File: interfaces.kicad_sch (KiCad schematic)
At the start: 84 parts, among them IC1 TPD8S009DSMR, J1 WE_629105150521, J2 685119134923, J3 1140084168, Q1 BSS138APW, Q2 BSS138APW, Q3 BSS138APW, Q4 BSS138APW, Q5 BSS138APW, U4 FT4232H-56Q, Y1 ABM8G-12.000MHZ-18-D2Y-T

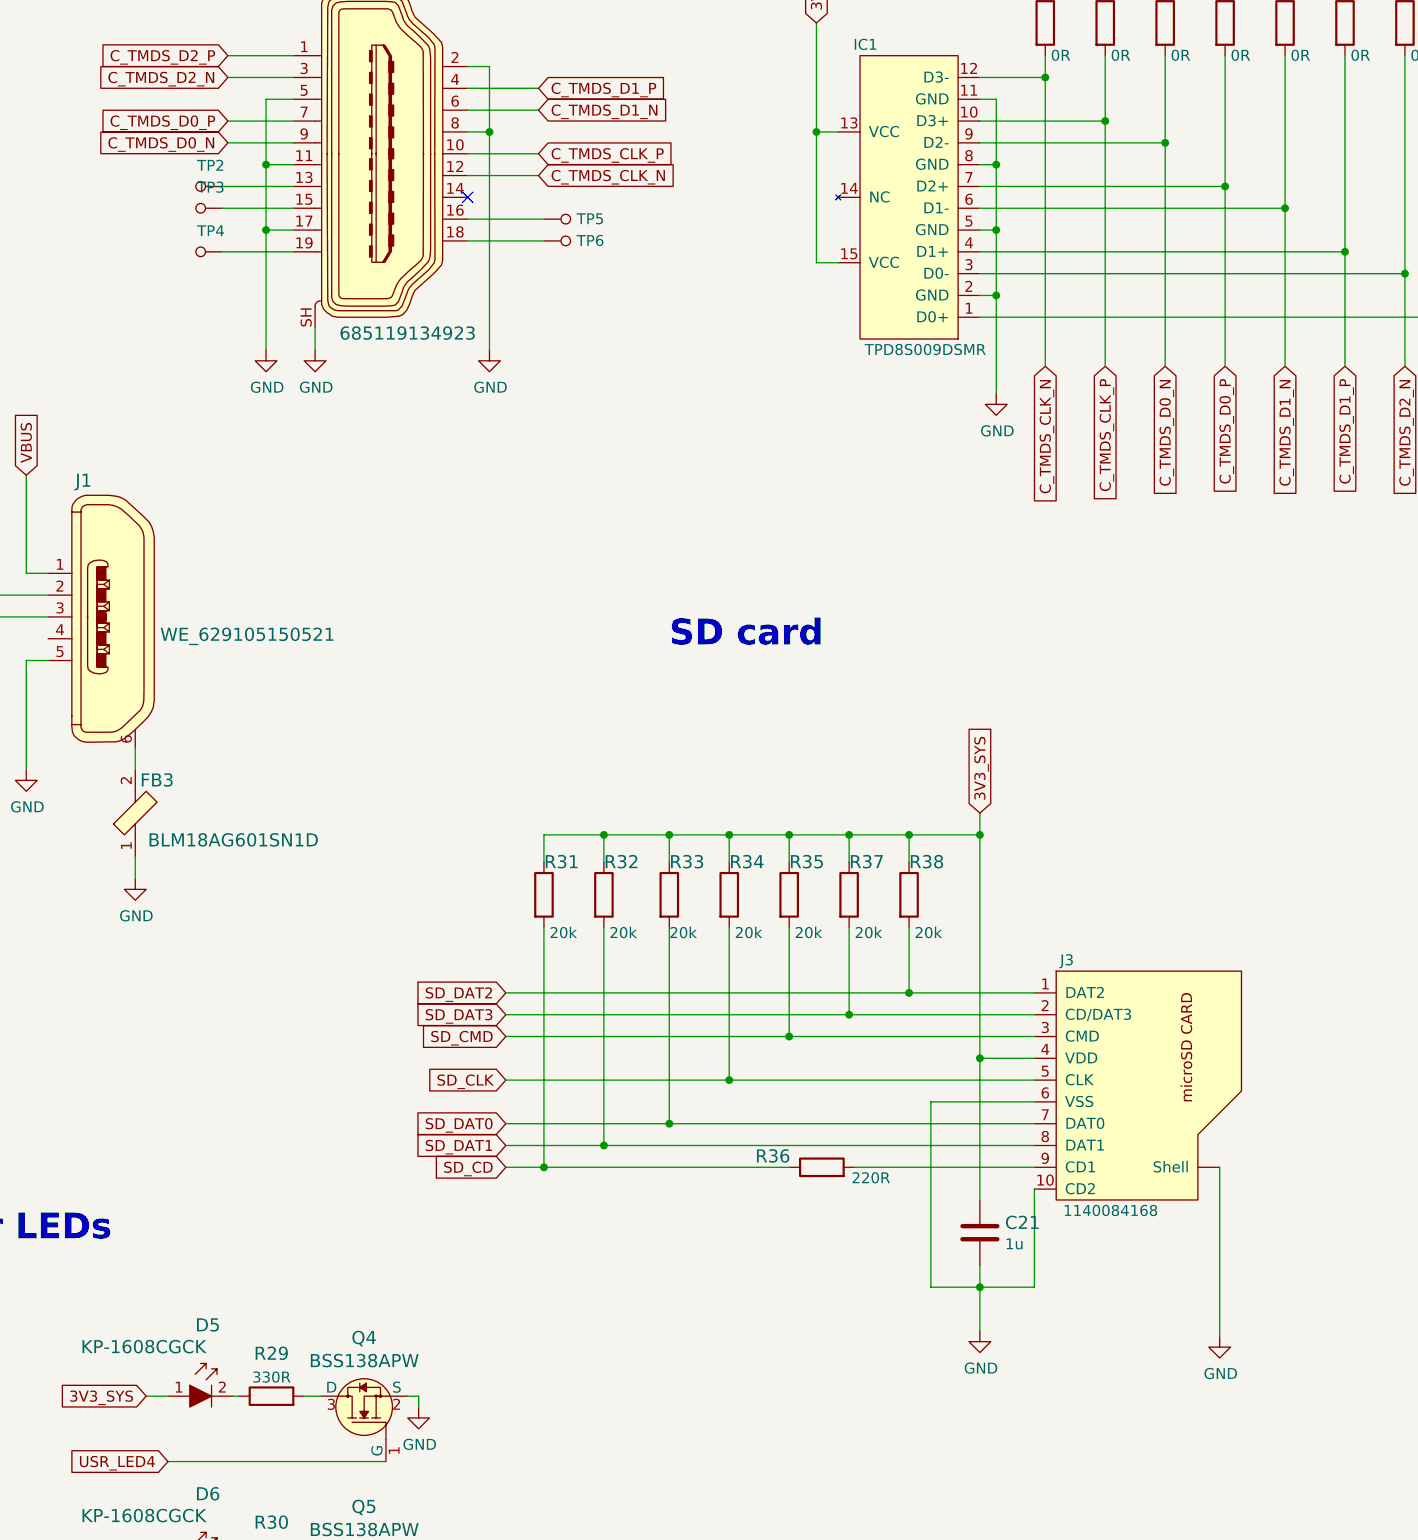
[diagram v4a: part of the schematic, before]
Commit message: Fix uSC symbol
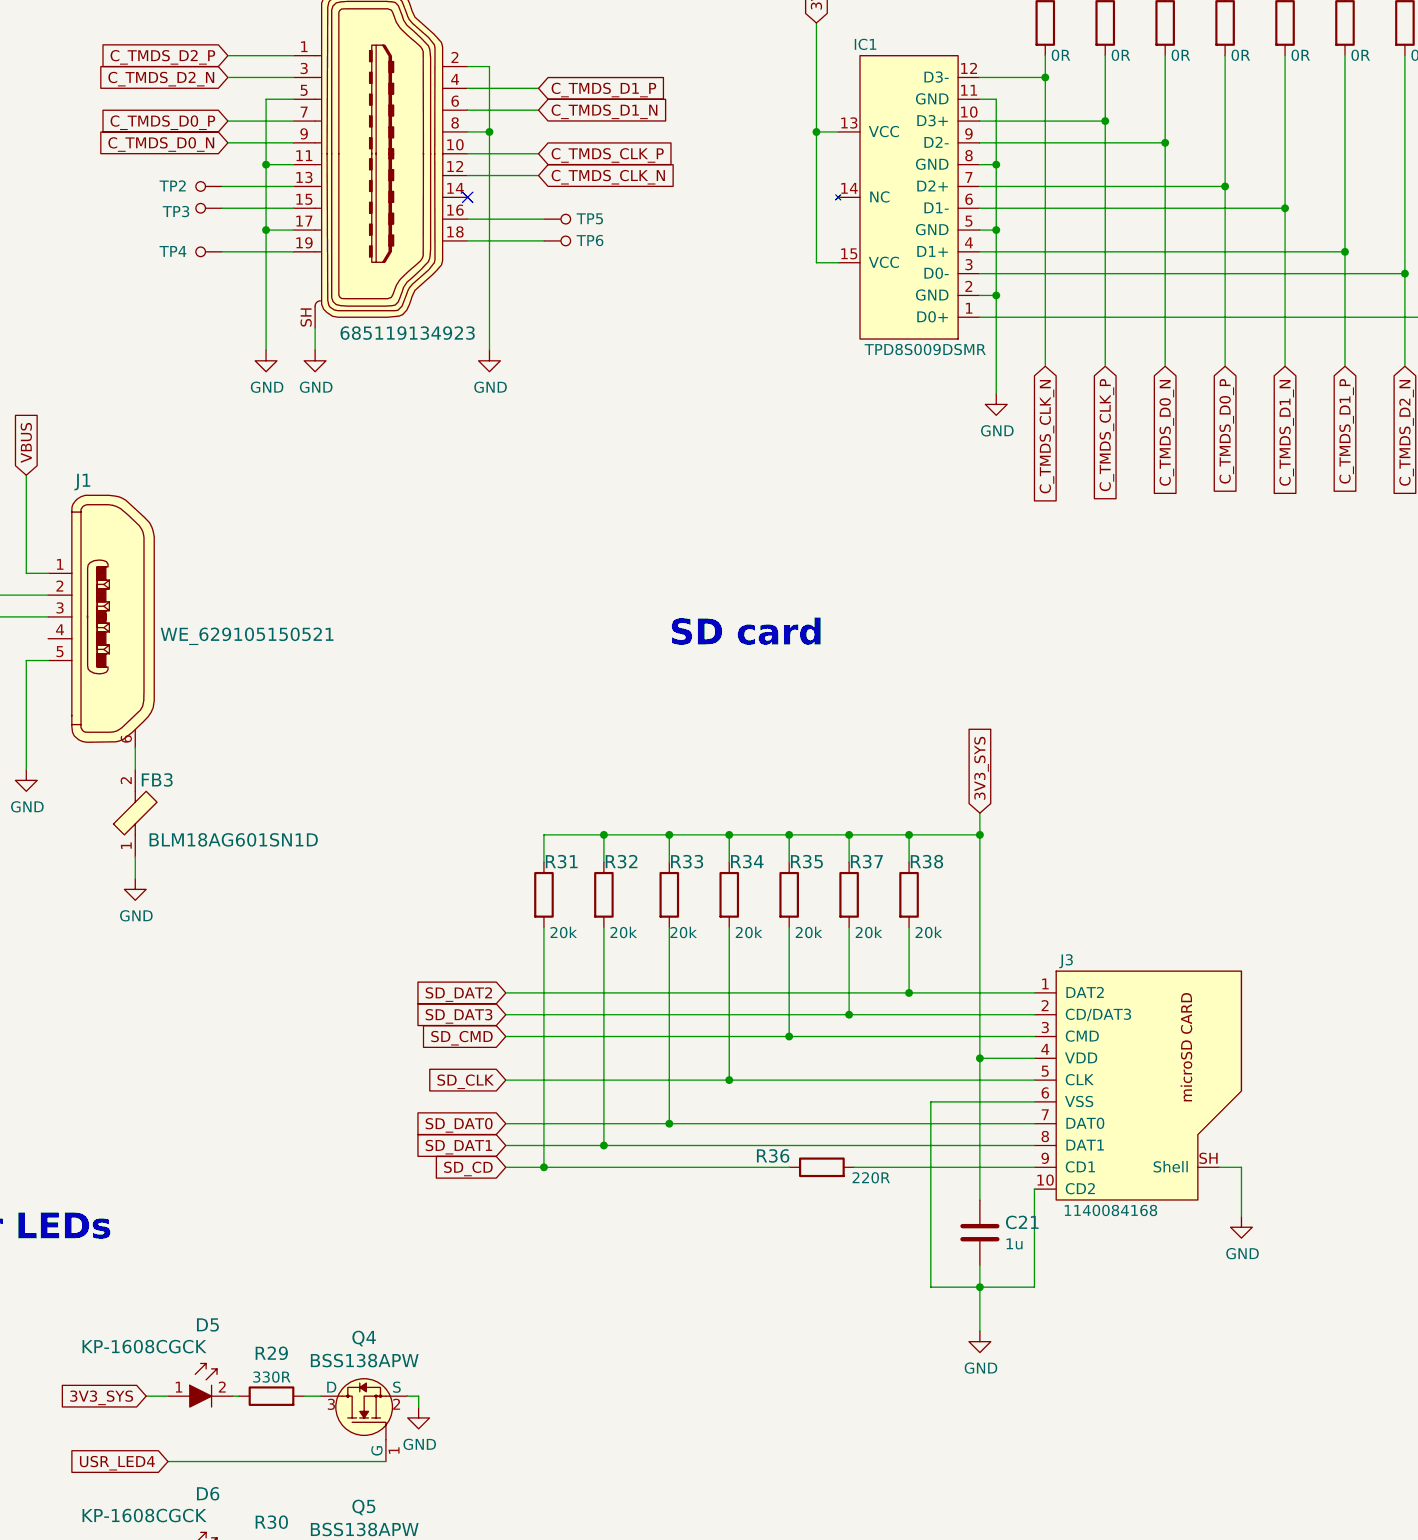
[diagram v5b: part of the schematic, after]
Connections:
- net GND: now also J3.SH (Shell); no longer J3.~ (Shell)
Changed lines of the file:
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@@
     (stroke (width 0) (type default) (color 0 0 0 0))
   )
-  (wire (pts (xy 365.76 197.485) (xy 365.76 217.17))
-    (stroke (width 0) (type default) (color 0 0 0 0))
-  )
   (wire (pts (xy 62.23 166.37) (xy 62.23 172.72))
     (stroke (width 0) (type default) (color 0 0 0 0))
@@
     (stroke (width 0) (type default) (color 0 0 0 0))
   )
+  (wire (pts (xy 368.3 197.485) (xy 368.3 203.2))
+    (stroke (width 0) (type default) (color 0 0 0 0))
+  )
   (wire (pts (xy 146.05 143.51) (xy 158.115 143.51))
     (stroke (width 0) (type default) (color 0 0 0 0))
@@
     (stroke (width 0) (type default) (color 0 0 0 0))
   )
+  (wire (pts (xy 368.3 197.485) (xy 365.76 197.485))
+    (stroke (width 0) (type default) (color 0 0 0 0))
+  )
   (wire (pts (xy 254.635 73.025) (xy 254.635 80.645))
     (stroke (width 0) (type default) (color 0 0 0 0))
@@
   (symbol (lib_id "lpddr4-test-board:TP_SMD1MM") (at 247.015 83.185 270) (unit 1)
     (in_bom yes) (on_board yes)
-    (property "Reference" "TP2" (id 0) (at 248.2088 80.772 90))
+    (property "Reference" "TP2" (id 0) (at 243.84 83.185 90))
     (property "Value" "TP_SMD1MM" (id 1) (at 244.475 83.185 0)
       (effects (font (size 1.27 1.27)) hide)
@@
   )
   (symbol (lib_id "lpddr4-test-board:TP_SMD1MM") (at 247.015 85.725 270) (unit 1)
-    (in_bom yes) (on_board yes)
-    (property "Reference" "TP3" (id 0) (at 248.2088 83.312 90))
+    (in_bom yes) (on_board yes) (fields_autoplaced)
+    (property "Reference" "TP3" (id 0) (at 245.8213 86.1588 90)
+      (effects (font (size 1.27 1.27)) (justify right))
+    )
     (property "Value" "TP_SMD1MM" (id 1) (at 244.475 85.725 0)
       (effects (font (size 1.27 1.27)) hide)
@@
   (symbol (lib_id "lpddr4-test-board:TP_SMD1MM") (at 247.015 90.805 270) (unit 1)
     (in_bom yes) (on_board yes)
-    (property "Reference" "TP4" (id 0) (at 248.2088 88.392 90))
+    (property "Reference" "TP4" (id 0) (at 243.84 90.805 90))
     (property "Value" "TP_SMD1MM" (id 1) (at 244.475 90.805 0)
       (effects (font (size 1.27 1.27)) hide)
@@
     (pin "8")
     (pin "9")
-    (pin "~")
+    (pin "SH")
   )
   (symbol (lib_id "lpddr4-test-board:R_20k_0402") (at 329.565 165.735 270) (unit 1)
@@
     (pin "1")
   )
-  (symbol (lib_id "lpddr4-test-board:GND") (at 365.76 217.17 0) (unit 1)
-    (in_bom yes) (on_board yes)
-    (property "Reference" "#PWR044" (id 0) (at 365.76 223.52 0)
-      (effects (font (size 1.27 1.27)) hide)
-    )
-    (property "Value" "GND" (id 1) (at 365.887 221.5642 0))
-    (property "Footprint" "" (id 2) (at 365.76 217.17 0)
-      (effects (font (size 1.27 1.27)) hide)
-    )
-    (property "Datasheet" "" (id 3) (at 365.76 217.17 0)
-      (effects (font (size 1.27 1.27)) hide)
-    )
-    (pin "1")
-  )
   (symbol (lib_id "lpddr4-test-board:BSS138APW") (at 210.82 224.155 90) (unit 1)
     (in_bom yes) (on_board yes)
@@
       (effects (font (size 1.27 1.27)) hide)
     )
+    (pin "1")
+  )
+  (symbol (lib_id "lpddr4-test-board:GND") (at 368.3 203.2 0) (unit 1)
+    (in_bom yes) (on_board yes)
+    (property "Reference" "#PWR0195" (id 0) (at 368.3 209.55 0)
+      (effects (font (size 1.27 1.27)) hide)
+    )
+    (property "Value" "GND" (id 1) (at 368.427 207.5942 0))
+    (property "Footprint" "" (id 2) (at 368.3 203.2 0)
+      (effects (font (size 1.27 1.27)) hide)
+    )
+    (property "Datasheet" "" (id 3) (at 368.3 203.2 0)
+      (effects (font (size 1.27 1.27)) hide)
+    )
